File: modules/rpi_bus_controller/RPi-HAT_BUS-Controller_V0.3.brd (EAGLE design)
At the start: 65 x 56 mm, 64 parts, among them IC1 MC34063AD, IC2 ADUM1201ARZ, IC3 P89LPC922FDH,512FDH, IC4 24LC-I/OT, IC5 LPC1115, Q1 ASF1, T1 BC856, T2 BCP52, T3 BC847

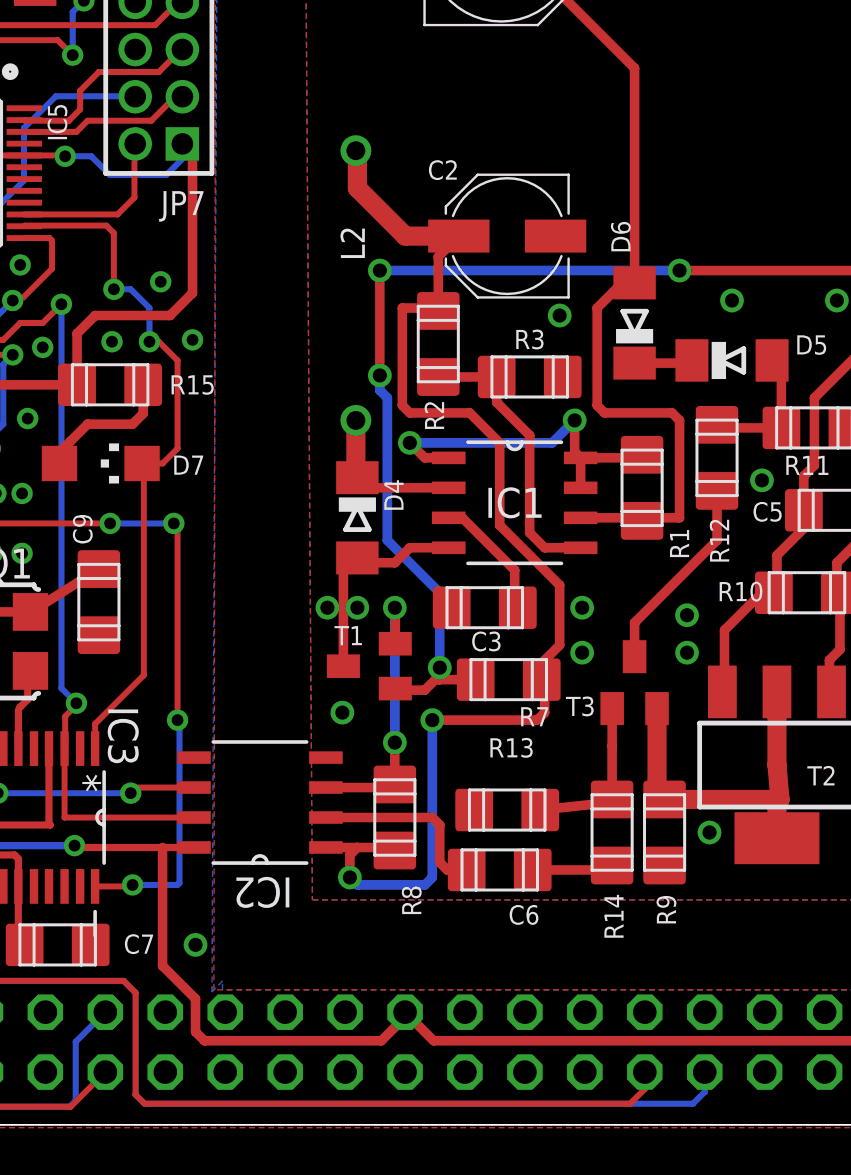
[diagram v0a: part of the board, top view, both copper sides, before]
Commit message: TXD RXD getauscht
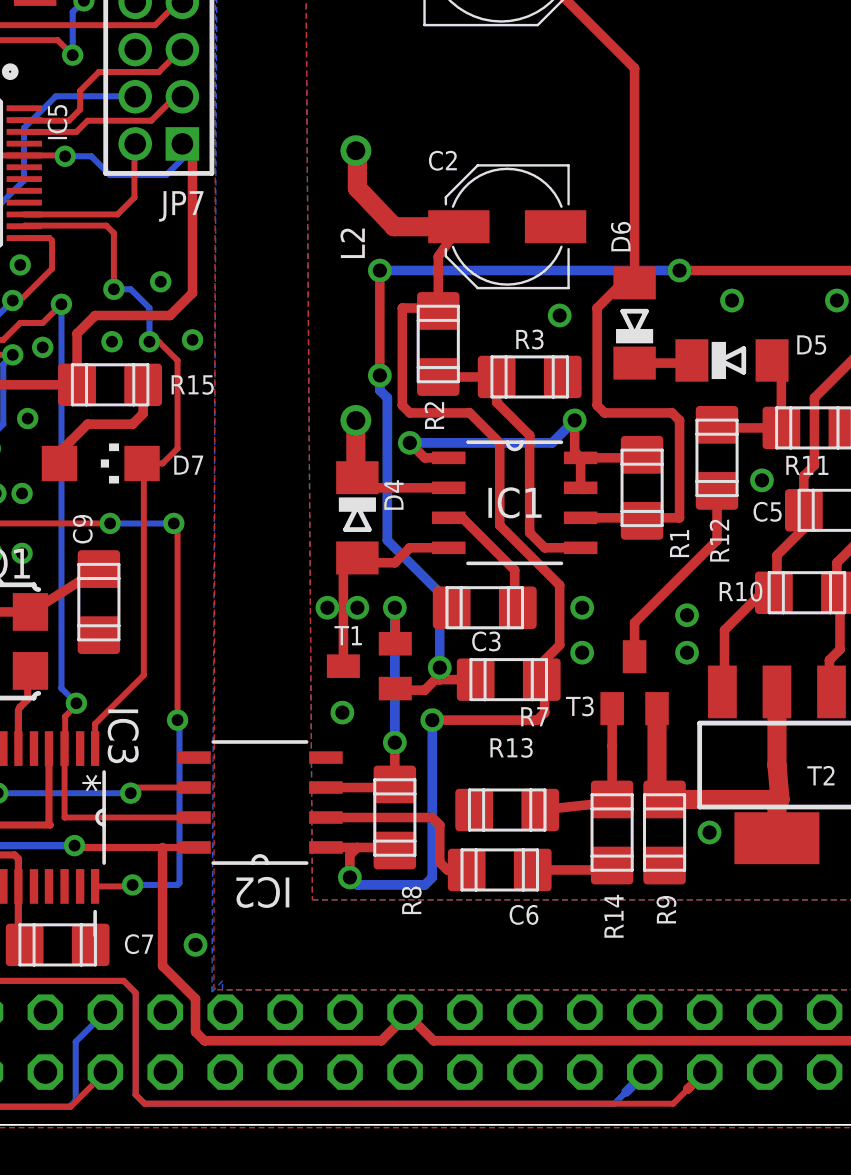
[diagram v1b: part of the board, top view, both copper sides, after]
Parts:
- moved C2 0.40 mm to (40.6, 38.1)
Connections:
- net RXD: now also JP2.8; no longer JP2.10
- net TXD: now also JP2.10; no longer JP2.8
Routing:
- net TXD: track 97.8 -> 94.8 mm
- net RXD: track 102.2 -> 104.3 mm
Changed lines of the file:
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@@
 </element>
 <element name="C1" library="RCL_for_Selfbus-Projects" package="PANASONIC_D" value="100µF" x="40.386" y="49.8475"/>
-<element name="C2" library="RCL_for_Selfbus-Projects" package="PANASONIC_C" value="100µF" x="40.64" y="37.6555" smashed="yes" rot="R180">
-<attribute name="NAME" x="38.6045" y="40.858625" size="0.8128" layer="25" font="vector" rot="R180"/>
-<attribute name="VALUE" x="42.734375" y="39.446125" size="0.8128" layer="27" font="vector" rot="R180"/>
+<element name="C2" library="RCL_for_Selfbus-Projects" package="PANASONIC_C" value="100µF" x="40.64" y="38.052375" smashed="yes" rot="R180">
+<attribute name="NAME" x="38.6045" y="41.2555" size="0.8128" layer="25" font="vector" rot="R180"/>
+<attribute name="VALUE" x="42.734375" y="39.843" size="0.8128" layer="27" font="vector" rot="R180"/>
 </element>
 <element name="C3" library="RCL_for_Selfbus-Projects" package="R1206" value="470p" x="39.6875" y="21.9075" smashed="yes" rot="R90">
@@
 <contactref element="R8" pad="2"/>
 <contactref element="IC2" pad="1"/>
-<wire x1="38.59" y1="37.6555" x2="36.322" y2="37.6555" width="0.8128" layer="1"/>
-<wire x1="36.322" y1="37.6555" x2="34.29" y2="39.6875" width="0.8128" layer="1"/>
+<wire x1="38.59" y1="38.052375" x2="35.84575" y2="38.052375" width="0.8128" layer="1"/>
+<wire x1="35.84575" y1="38.052375" x2="34.29" y2="39.6875" width="0.8128" layer="1"/>
 <wire x1="34.29" y1="39.6875" x2="34.29" y2="41.2115" width="0.8128" layer="1"/>
 <wire x1="34.29" y1="41.2115" x2="34.2265" y2="41.275" width="0.8128" layer="1"/>
 <wire x1="37.719" y1="34.4835" x2="37.719" y2="36.7845" width="0.4064" layer="1"/>
-<wire x1="37.719" y1="36.7845" x2="38.59" y2="37.6555" width="0.4064" layer="1"/>
+<wire x1="37.719" y1="36.7845" x2="38.59" y2="38.052375" width="0.4064" layer="1"/>
 <wire x1="32.9565" y1="11.7475" x2="34.29" y2="11.7475" width="0.4064" layer="1"/>
 <wire x1="34.29" y1="11.7475" x2="35.6205" y2="11.7475" width="0.4064" layer="1"/>
@@
 </signal>
 <signal name="TXD">
-<contactref element="JP2" pad="8"/>
 <contactref element="IC3" pad="12"/>
-<wire x1="49.01" y1="2.23" x2="49.01" y2="1.385" width="0.254" layer="16"/>
-<wire x1="49.01" y1="1.385" x2="48.514" y2="0.889" width="0.254" layer="16"/>
-<wire x1="48.514" y1="0.889" x2="25.273" y2="0.889" width="0.254" layer="16"/>
+<wire x1="45.67625" y1="1.385" x2="45.18025" y2="0.889" width="0.254" layer="16"/>
+<wire x1="45.18025" y1="0.889" x2="25.273" y2="0.889" width="0.254" layer="16"/>
 <wire x1="25.273" y1="0.889" x2="24.892" y2="1.27" width="0.254" layer="16"/>
 <wire x1="24.892" y1="1.27" x2="24.892" y2="5.588" width="0.254" layer="16"/>
@@
 <wire x1="9.763125" y1="18.811875" x2="9.763125" y2="15.08125" width="0.254" layer="16"/>
 <wire x1="9.763125" y1="15.08125" x2="12.144375" y2="12.7" width="0.254" layer="16"/>
+<contactref element="JP2" pad="10"/>
+<wire x1="46.47" y1="2.23" x2="46.47" y2="2.17875" width="0.4064" layer="16"/>
+<wire x1="46.47" y1="2.17875" x2="45.67625" y2="1.385" width="0.4064" layer="16"/>
 </signal>
 <signal name="RXD">
-<contactref element="JP2" pad="10"/>
 <contactref element="IC3" pad="11"/>
-<wire x1="46.47" y1="2.23" x2="46.47" y2="1.512" width="0.254" layer="1"/>
-<wire x1="46.47" y1="1.512" x2="45.847" y2="0.889" width="0.254" layer="1"/>
-<wire x1="45.847" y1="0.889" x2="25.273" y2="0.889" width="0.254" layer="1"/>
+<wire x1="48.295625" y1="1.512" x2="47.672625" y2="0.889" width="0.254" layer="1"/>
+<wire x1="47.672625" y1="0.889" x2="25.273" y2="0.889" width="0.254" layer="1"/>
 <wire x1="25.273" y1="0.889" x2="24.892" y2="1.27" width="0.254" layer="1"/>
 <wire x1="24.892" y1="1.27" x2="24.892" y2="5.588" width="0.254" layer="1"/>
@@
 <wire x1="3.96875" y1="20.955" x2="2.936875" y2="20.955" width="0.254" layer="16"/>
 <wire x1="2.936875" y1="20.955" x2="2.2225" y2="21.669375" width="0.254" layer="16"/>
+<contactref element="JP2" pad="8"/>
+<wire x1="48.295625" y1="1.512" x2="48.295625" y2="1.515625" width="0.4064" layer="1"/>
+<wire x1="48.295625" y1="1.515625" x2="49.01" y2="2.23" width="0.4064" layer="1"/>
 </signal>
 <signal name="ID_SC">

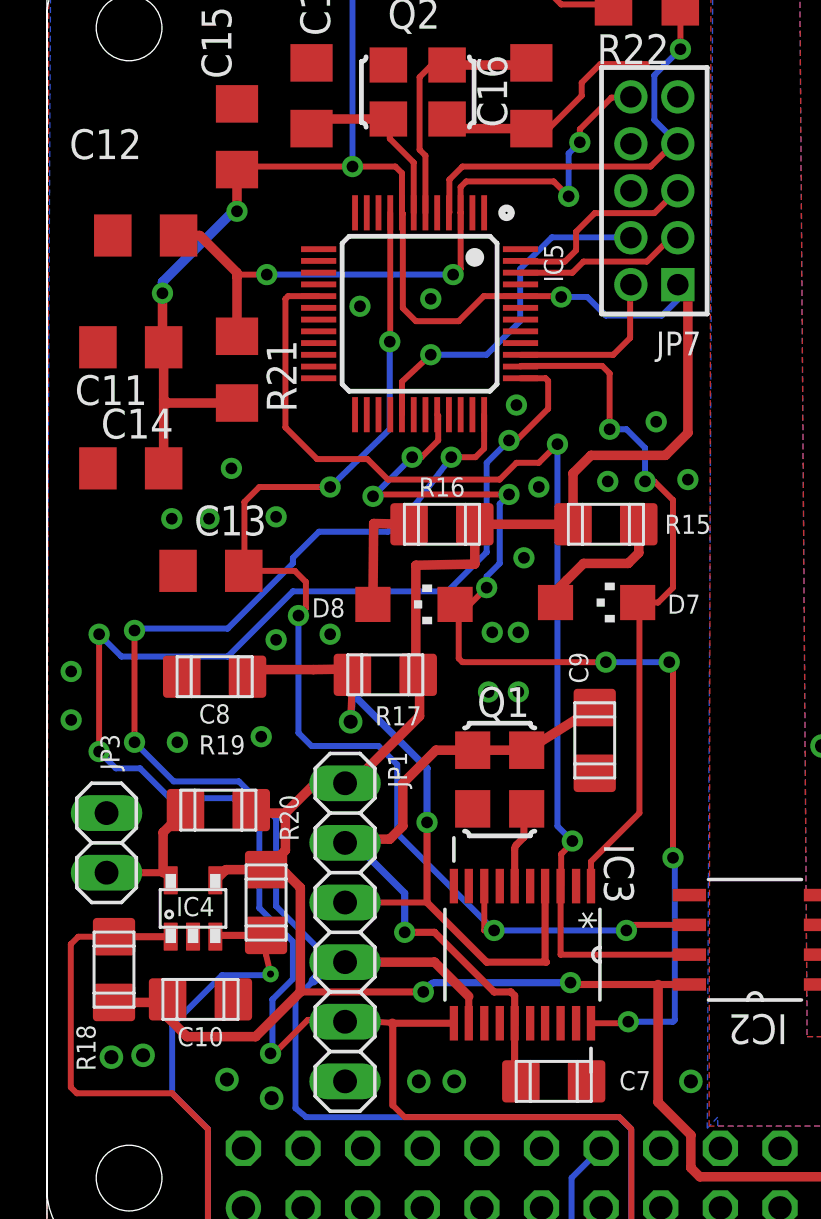
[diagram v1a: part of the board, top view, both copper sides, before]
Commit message: Schutzwiderstände in TXD_ARM und EIB-OUT_ARM eingefügt
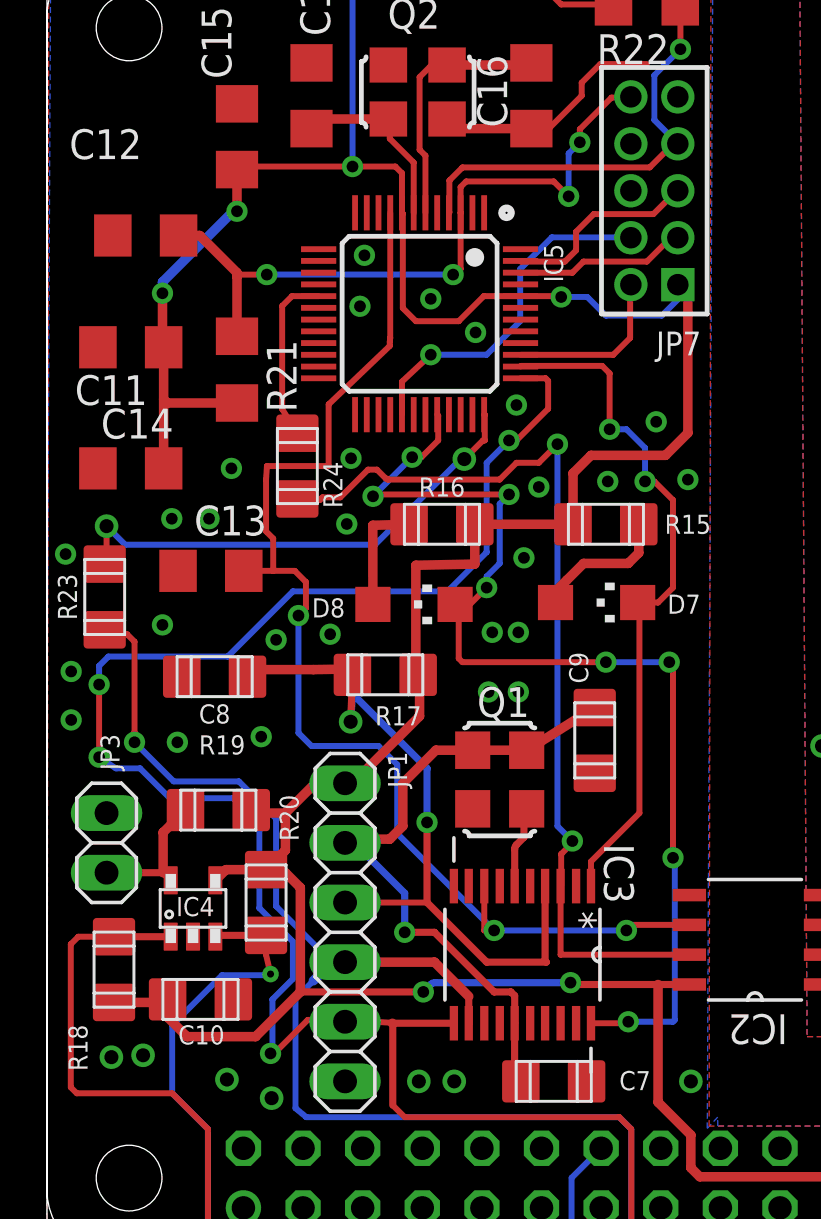
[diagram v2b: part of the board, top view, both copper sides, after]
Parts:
- added R23, R24: 330, RCL_for_Selfbus-Projects:R1206
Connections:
- new net EIBOUT_ARM: IC5.17, R24.2
- new net TXD_ARM: IC5.36, R23.1
- net EIB_OUT: now also R24.1; no longer IC5.17
- net TXD: now also R23.2; no longer IC5.36
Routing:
- net TXD_ARM: track 0.00 -> 21.1 mm, vias 0 -> 2
- net TXD: track 94.8 -> 76.0 mm, vias 3 -> 1
- net EIB_OUT: track 47.8 -> 40.1 mm
- net EIBOUT_ARM: track 0.00 -> 7.34 mm
- net RXD: track 104.3 -> 102.9 mm
- net EIB_IN: track 54.0 -> 53.0 mm, vias 5 -> 3
- net GND/2: vias 29 -> 34

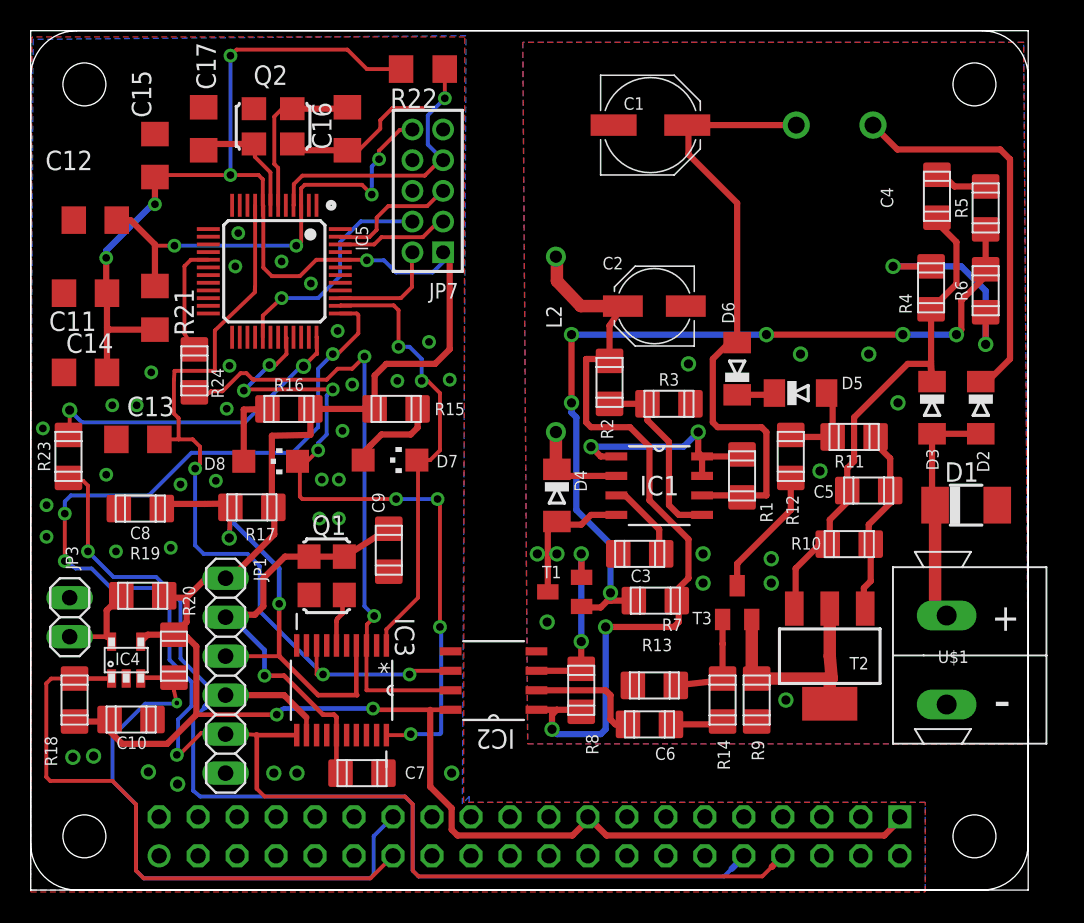
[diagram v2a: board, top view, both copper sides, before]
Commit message: schaltregler modifiziert, LEDs für ARM eingefügt und enable R für 922
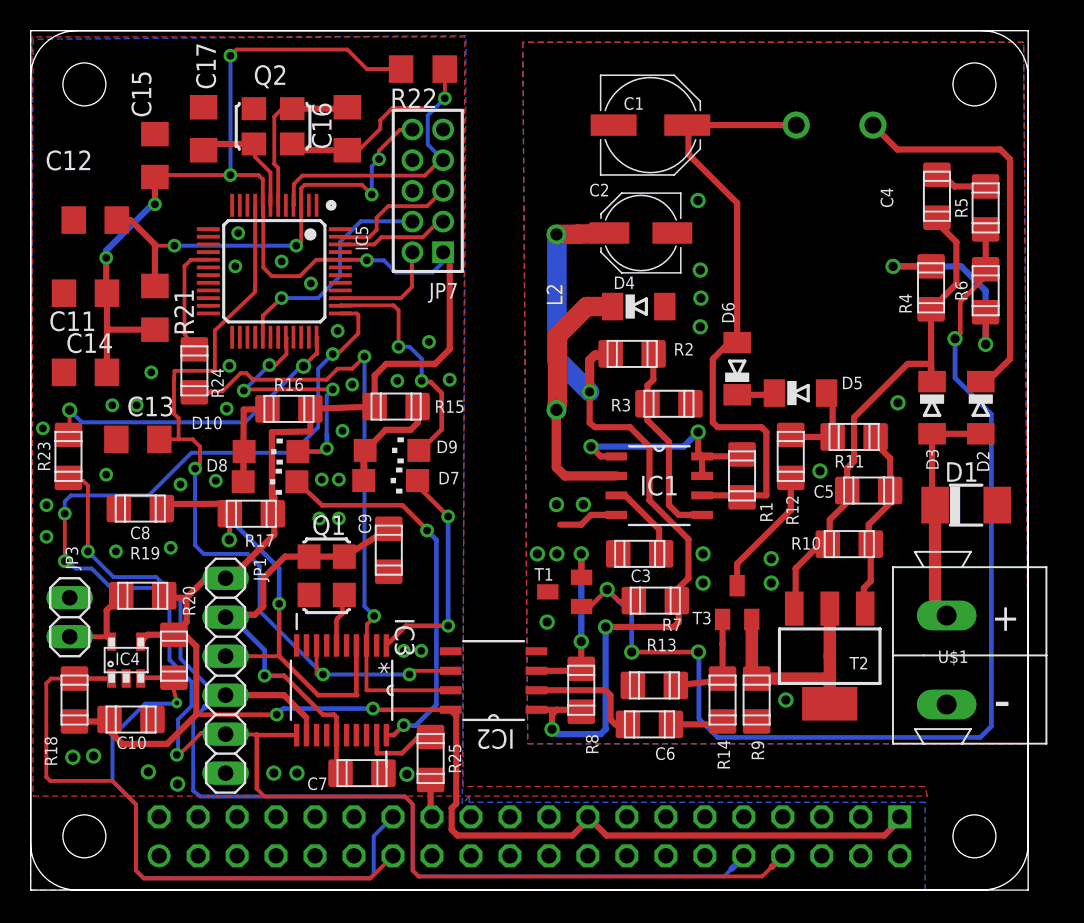
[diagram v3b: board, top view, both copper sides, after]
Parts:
- added D10: red, Diode_for_Selfbus-Projects:CHIPLED_1206
- added D9: green, Diode_for_Selfbus-Projects:CHIPLED_1206
- added R25: 1k, RCL_for_Selfbus-Projects:R1206
- moved D4 13.4 mm to (39.6, 38.0), turned to 0 degrees
- moved C2 4.84 mm to (39.8, 42.8)
- moved R2 2.37 mm to (39.2, 34.9), turned to 270 degrees
- moved L2 1.45 mm to (34.3, 37.0)
- moved D7 1.33 mm to (23.5, 26.7)
- moved D8 1.33 mm to (15.6, 26.6)
- moved R17 0.42 mm to (14.4, 24.5)
- moved R15 0.15 mm to (23.8, 31.5)
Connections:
- new net N$11: D7.C, IC3.1
- new net N$14: IC3.19, R25.2
- new net N$9: D8.C, IC3.20
- net GND/2: now also R25.1
- net IO12: now also D10.C; no longer D8.C, IC3.20
- net IO15: now also D9.C; no longer D7.C, IC3.1
- net N$35: now also D9.A
- net N$38: now also D10.A
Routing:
- net IO12: track 47.1 -> 16.7 mm, vias 8 -> 4
- net N$9: track 0.00 -> 25.5 mm, vias 0 -> 2
- net N$6: track 54.7 -> 71.7 mm, vias 6 -> 4
- net N$11: track 0.00 -> 14.9 mm, vias 0 -> 2
- net IO15: track 29.6 -> 15.6 mm
- net N$13: track 6.54 -> 17.1 mm
- net N$14: track 0.00 -> 5.13 mm
- net GND: track 23.8 -> 18.7 mm, vias 15 -> 18
- net +3V3: track 53.5 -> 57.3 mm, vias 2 -> 3
- net N$35: track 5.92 -> 9.24 mm
- net N$38: track 4.92 -> 8.23 mm
- net GND/2: track 10.8 -> 13.3 mm, vias 34 -> 36
- net N$3: track 12.1 -> 13.0 mm
- net RST: track 30.9 -> 31.4 mm
